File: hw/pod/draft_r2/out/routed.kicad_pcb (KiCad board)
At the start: 4 copper layers, 30 x 12 mm, 74 parts, among them J1 TestPoint_Pad_D1.0mm, J10 TestPoint_Pad_D1.0mm, J11 TestPoint_Pad_D1.0mm, J12 TestPoint_Pad_D1.0mm, J2 TestPoint_Pad_D1.0mm, J3 TestPoint_Pad_D1.0mm, J4 WirePad_1.0x2.0mm, J5 TestPoint_Pad_D1.0mm, J7 TestPoint_Pad_D1.0mm, J8 TestPoint_Pad_D1.0mm, J9 TestPoint_Pad_D1.0mm, Q1 Nexperia_SOT1216_DFN1010B-6, Q2 Nexperia_SOT1216_DFN1010B-6, SW1 SW-SMD_4P-L3.0-W2.6-P1.85-LS3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, U1 QFN-48-1EP_7x7mm_P0.5mm_EP5.6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, U2 Knowles_LGA-5_3.5x2.65mm, U3 DSBGA-8_L1.6-W0.9-R2-C4-P0.40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, U4 X2SON-4_L1.0-W1.0-P0.65-TL-EP, U6 SOT-553-5_L1.6-W1.2-P0.50-LS1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, Y1 Crystal_SMD_2012-2Pin_2.0x1.2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

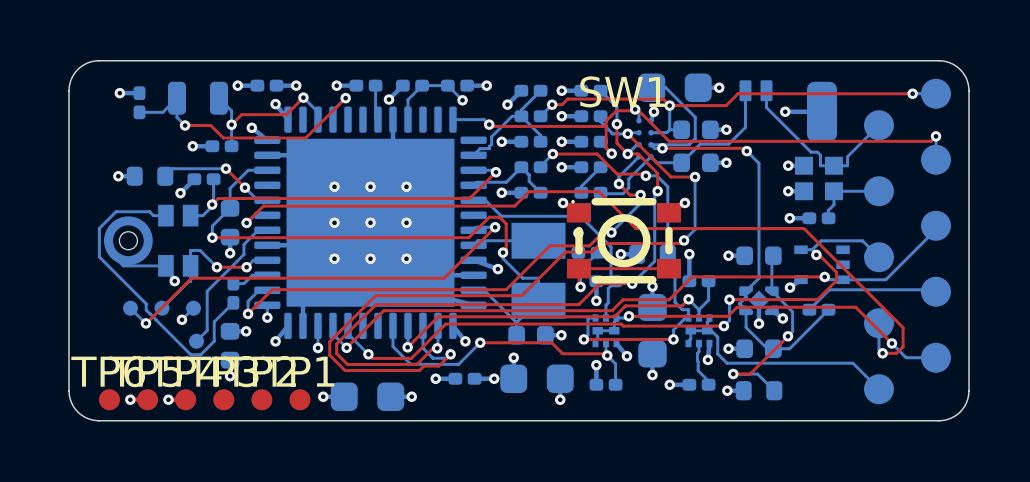
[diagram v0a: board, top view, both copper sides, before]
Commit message: Phase 2 route: 0.11 mm routing clearance for both FreeRouting passes (0.10 produced 0.192 mm hole clearance); routed board DRC 0 errors, 7 unconnected (U1 top-row escapes NRST/BTN/VBUS_SENSE + LSE_OUT, MDF_CCK, TP1/TP6): needs U1's top strip (C1/C10/C2/C3) loosened or hand routing
Co-Authored-By: Claude Opus 5.5 <noreply@anthropic.com>
Claude-Session: https://claude.ai/code/session_01Wg997D6KFs8bxoAH56jZZJ
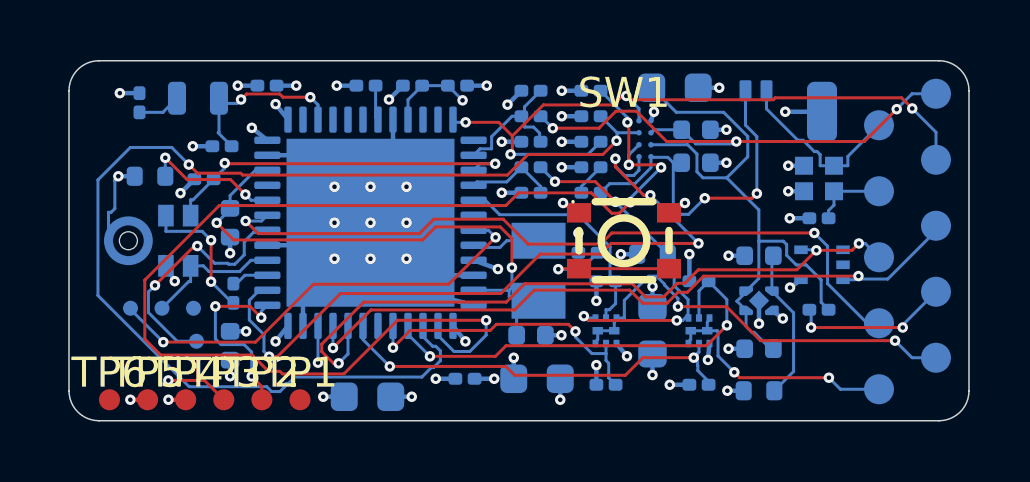
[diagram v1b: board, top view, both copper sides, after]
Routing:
- net I2C_SCL: track 23.8 -> 41.6 mm
- net GB_P: track 1.55 -> 13.9 mm, vias 0 -> 2
- net I2C_SDA: track 26.7 -> 38.9 mm, vias 4 -> 2
- net LSE_OUT: track 9.43 -> 1.44 mm, vias 2 -> 0
- net CHG_INT: track 18.2 -> 24.6 mm
- net SWCLK: track 0.41 -> 6.39 mm, vias 1 -> 3
- net MIC_CLK: track 10.5 -> 4.57 mm, vias 0 -> 2
- net VBUS: track 7.32 -> 11.7 mm, vias 0 -> 2
- net DBG_TX: track 4.86 -> 8.26 mm, vias 0 -> 2
- net TS: track 19.8 -> 23.2 mm
- net BRIDGE_RTN: track 14.7 -> 11.9 mm
- net LED_K: track 27.5 -> 24.8 mm
- net VSYS: track 17.4 -> 19.8 mm, vias 2 -> 0
- net VBAT: track 15.5 -> 17.8 mm
- net GB_N: track 12.6 -> 14.7 mm
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
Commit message: Phase 2 board lettering: silk.py reads the port/button/outline from the board (one-face board: name block between the mic-port motif and SW1, 'PHASE 2'); pin-1 dot list in a sidecar; place_r2 --route letters the fresh board. Known issue: manual re-runs on an already-lettered board can segfault in pcbnew's SWIG bindings (build scripts only letter fresh boards)
Co-Authored-By: Claude Opus 5.5 <noreply@anthropic.com>
Claude-Session: https://claude.ai/code/session_01Wg997D6KFs8bxoAH56jZZJ
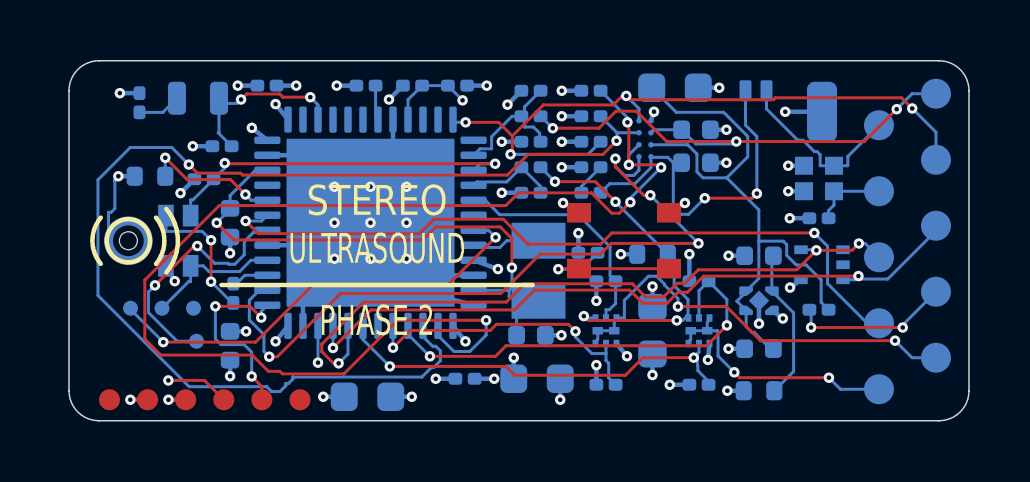
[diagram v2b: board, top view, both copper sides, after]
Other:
- board text added: "PHASE 2"
- board text added: "STEREO"
- board text added: "ULTRASOUND"

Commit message: Phase 2 route closure (agent v6): 1 unconnected (I2C_SCL at U1.26), DRC 0 errors, placement check pass: U1 top strip loosened (C2/C3/C10), C9 pocket fixed, Y1 vertical, TP3/TP6 moved on F; mic port now x 1.88 (shell_r2 re-check)
Co-Authored-By: Claude Opus 5.5 <noreply@anthropic.com>
Claude-Session: https://claude.ai/code/session_01Wg997D6KFs8bxoAH56jZZJ
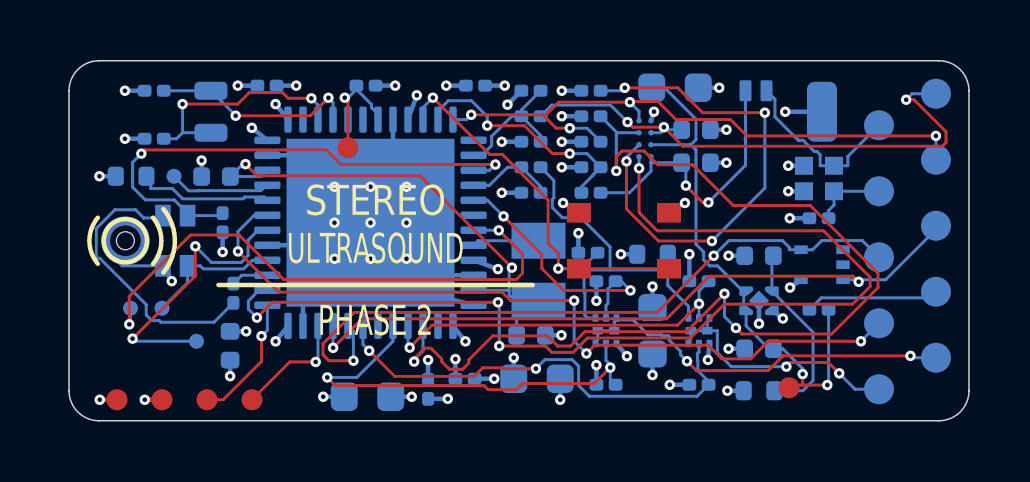
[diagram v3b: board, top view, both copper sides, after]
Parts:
- moved TP6 22.7 mm to (24.0, 10.9)
- moved C2 10.1 mm to (12.0, 10.9), turned to -90 degrees
- moved TP3 9.36 mm to (9.30, 2.90)
- moved TP8 4.45 mm to (3.50, 3.85)
- moved C11 2.27 mm to (2.84, 2.60)
- moved TP2 1.83 mm to (4.60, 11.3)
- moved C9 1.61 mm to (4.90, 3.86), turned to 180 degrees
- moved TP1 1.60 mm to (6.10, 11.3)
- moved C13 1.58 mm to (5.12, 5.40), turned to -90 degrees
- moved TP5 1.02 mm to (1.60, 11.3)
- moved TP4 0.79 mm to (3.10, 11.3)
- moved C12 0.63 mm to (2.84, 1.00), turned to 180 degrees
- moved R1 0.63 mm to (2.07, 3.85)
- moved Y1 0.62 mm to (4.73, 1.70), turned to 90 degrees
- moved C3 0.60 mm to (13.6, 0.83)
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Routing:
- net I2C_SCL: track 41.6 -> 16.5 mm, vias 5 -> 4
- net CHG_INT: track 24.6 -> 35.3 mm
- net BTN: track 5.24 -> 13.8 mm, vias 1 -> 2
- net VBUS_SENSE: track 1.12 -> 8.06 mm, vias 0 -> 2
- net MIC_VDD: track 12.1 -> 17.6 mm
- net LSE_OUT: track 1.44 -> 6.87 mm, vias 0 -> 2
- net MIC_CLK: track 4.57 -> 9.54 mm, vias 2 -> 0
- net GA_P: track 10.2 -> 14.6 mm
- net I2C_SDA: track 38.9 -> 34.6 mm, vias 2 -> 4
- net MDF_SDI: track 14.9 -> 18.7 mm
- net MDF_CCK: track 0.00 -> 3.39 mm
- net SWDIO: track 1.23 -> 3.88 mm
- net TS: track 23.2 -> 20.6 mm
- net GB_N: track 14.7 -> 12.4 mm
- net VBUS: track 11.7 -> 9.52 mm
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
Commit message: Phase 2 board fully routed: 0 unconnected, DRC 0. I2C_SCL at U1.26 (boxed in on both outer faces) bridged 8.97 mm on the In2 +3V0 plane by new hw/pod/inner_bridge.py (maze route, plane stays one island, -4 mm2). Pin swap ruled out from the DS AF table; ECR-0018 log + reg-board updated
Co-Authored-By: Claude Opus 5.5 <noreply@anthropic.com>
Claude-Session: https://claude.ai/code/session_01Wg997D6KFs8bxoAH56jZZJ
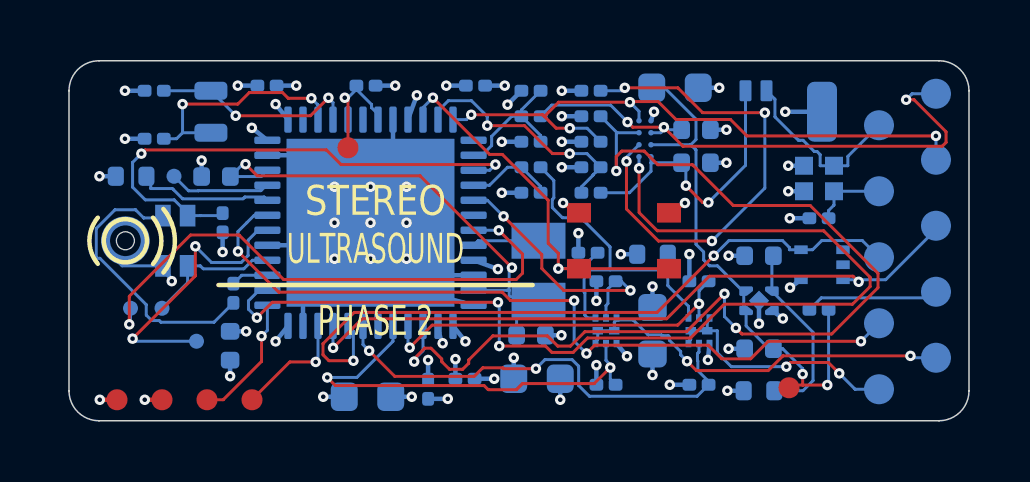
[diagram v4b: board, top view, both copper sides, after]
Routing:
- net I2C_SCL: track 16.5 -> 26.1 mm, vias 4 -> 5
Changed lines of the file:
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@@
+	)
+	(via
+		(at 12.455291 9.417055)
+		(size 0.35)
+		(drill 0.15)
+		(layers "F.Cu" "B.Cu")
+		(net "I2C_SCL")
 	)
 	(via
@@
 		(drill 0.15)
 		(layers "F.Cu" "B.Cu")
+		(net "I2C_SCL")
+	)
+	(segment
+		(start 12.3 8.8375)
+		(end 12.455291 9.417055)
+		(width 0.1)
+		(layer "B.Cu")
 		(net "I2C_SCL")
 	)
@@
 		(net "I2C_SCL")
 	)
+	(segment
+		(start 18.575 3.775)
+		(end 18.625 3.725)
+		(width 0.1)
+		(layer "In2.Cu")
+		(net "I2C_SCL")
+	)
+	(segment
+		(start 14.175 7.725)
+		(end 14.225 7.675)
+		(width 0.1)
+		(layer "In2.Cu")
+		(net "I2C_SCL")
+	)
+	(segment
+		(start 18.575 3.875)
+		(end 18.575 3.775)
+		(width 0.1)
+		(layer "In2.Cu")
+		(net "I2C_SCL")
+	)
+	(segment
+		(start 12.455291 9.417055)
+		(end 12.475 9.375)
+		(width 0.1)
+		(layer "In2.Cu")
+		(net "I2C_SCL")
+	)
+	(segment
+		(start 12.475 9.375)
+		(end 14.125 7.725)
+		(width 0.1)
+		(layer "In2.Cu")
+		(net "I2C_SCL")
+	)
+	(segment
+		(start 16.775 5.425)
+		(end 16.825 5.425)
+		(width 0.1)
+		(layer "In2.Cu")
+		(net "I2C_SCL")
+	)
+	(segment
+		(start 18.625 3.425)
+		(end 18.5827 3.353)
+		(width 0.1)
+		(layer "In2.Cu")
+		(net "I2C_SCL")
+	)
+	(segment
+		(start 14.125 7.725)
+		(end 14.175 7.725)
+		(width 0.1)
+		(layer "In2.Cu")
+		(net "I2C_SCL")
+	)
+	(segment
+		(start 14.225 7.675)
+		(end 14.525 7.675)
+		(width 0.1)
+		(layer "In2.Cu")
+		(net "I2C_SCL")
+	)
+	(segment
+		(start 17.075 5.375)
+		(end 18.575 3.875)
+		(width 0.1)
+		(layer "In2.Cu")
+		(net "I2C_SCL")
+	)
+	(segment
+		(start 14.525 7.675)
+		(end 16.775 5.425)
+		(width 0.1)
+		(layer "In2.Cu")
+		(net "I2C_SCL")
+	)
+	(segment
+		(start 16.875 5.375)
+		(end 17.075 5.375)
+		(width 0.1)
+		(layer "In2.Cu")
+		(net "I2C_SCL")
+	)
+	(segment
+		(start 16.825 5.425)
+		(end 16.875 5.375)
+		(width 0.1)
+		(layer "In2.Cu")
+		(net "I2C_SCL")
+	)
+	(segment
+		(start 18.625 3.725)
+		(end 18.625 3.425)
+		(width 0.1)
+		(layer "In2.Cu")
+		(net "I2C_SCL")
+	)

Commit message: LN-M03 Kelvin fix on the Phase-2 board: hw/pod/kelvin_r21.py (two pad-hugging GND vias at R21, 4 options scored). All layout-noise metrics now pass (M03 3.31 -> 1.29 %); DRC 0, 0 unconnected
Co-Authored-By: Claude Opus 5.5 <noreply@anthropic.com>
Claude-Session: https://claude.ai/code/session_01Wg997D6KFs8bxoAH56jZZJ
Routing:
- net GND: track 38.7 -> 38.9 mm, vias 48 -> 49
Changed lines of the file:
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@@
+	)
+	(via
+		(at 18.94 6.01)
+		(size 0.35)
+		(drill 0.15)
+		(layers "F.Cu" "B.Cu")
+		(net "GND")
+	)
+	(via
+		(at 18.55 6.45)
+		(size 0.35)
+		(drill 0.15)
+		(layers "F.Cu" "B.Cu")
+		(net "GND")
 	)
 	(via
@@
 	(via
 		(at 10.875 0.83)
-		(size 0.35)
-		(drill 0.15)
-		(layers "F.Cu" "B.Cu")
-		(net "GND")
-	)
-	(via
-		(at 18.395 6.45)
 		(size 0.35)
 		(drill 0.15)
@@
 	)
 	(segment
-		(start 18.94 6.45)
-		(end 18.395 6.45)
-		(width 0.15)
-		(layer "B.Cu")
-		(net "GND")
-	)
-	(segment
 		(start 10.22 0.83)
 		(end 10.875 0.83)
@@
 	)
 	(segment
+		(start 18.94 6.45)
+		(end 18.94 6.01)
+		(width 0.25)
+		(layer "B.Cu")
+		(net "GND")
+	)
+	(segment
 		(start 24.5 3.5)
 		(end 23.975 3.5)
@@
 		(layer "B.Cu")
 		(net "GND")
+	)
+	(segment
+		(start 18.94 6.45)
+		(end 18.55 6.45)
+		(width 0.25)
+		(layer "B.Cu")
+		(net "GND")

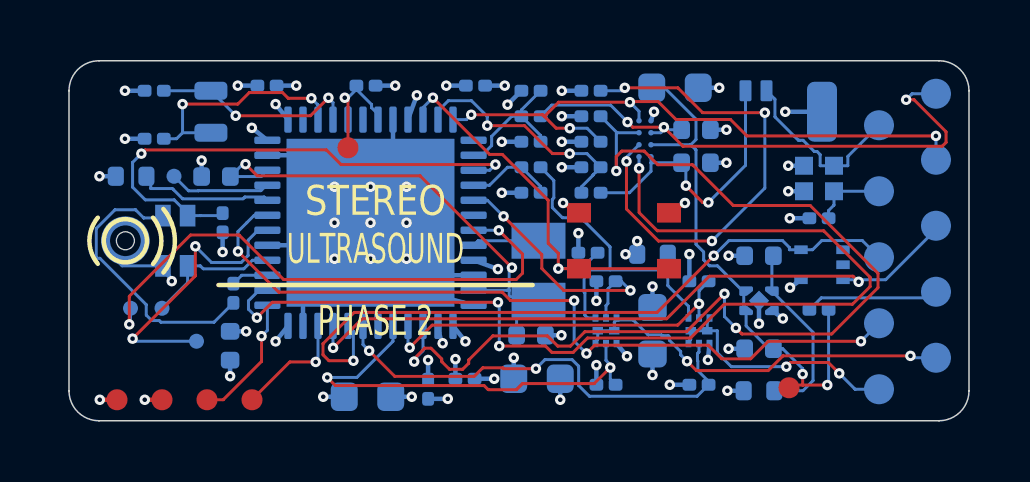
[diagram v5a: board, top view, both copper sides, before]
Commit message: Phase-2 board: B-DOC-AUDIT-0007 layout fixes 1-3 (local re-route of the committed board)
- J3 DOCK_VBUS / J4 GND swapped: J4 now sits between J3 and J5 VBAT (ASM-09); J3-J5 gap 1.17 -> 2.80 mm, all wire-pad gaps >= 0.90
- mic-port keep-out (R-ACO-P6): F.Cu rule area r 1.6 in place_r2 (FreeRouting + DRC enforce it), fan-out avoids it, check 'port';
  MDF_SDI re-routed: nearest F copper / via 1.35 -> 1.87 mm from the port
- LSE: Y1/C11/C12 moved, C1 to the QFN corner; LSE_IN/LSE_OUT pre-routed on B (locked), 0 vias, 7.72 / 7.43 mm (was 2 vias each, F+B)
- VDDA pin 9: C6 100 nF at the pin (1.13 mm, was 8.8), C5 1 uF 2.32 mm (was 9.2); C3 to VDD pin 36; C10 / R9 nudged; NEAR rules per pin
- R21 stays mid-board (MZD-4 not done): edge position scored LN-M03 2.48 % (limit 2) or an unroutable BRIDGE_RTN when flipped
- tools: place_r2 pre-routes / keep-out / --probe / --fr-args; local_reroute.py (move + rip + locked FreeRouting pass);
  fb_bridge.py (F+B maze, rip-and-repair); inner_bridge F/B layers + pads/rule areas as obstacles; kelvin_r21 reads the R21 pad
- DRC 0 / 0 unconnected; place_r2 check pass; LN M01..M05 26.5 / 20.1 / 1.29 % / 0.127 / 8.72 (unchanged); smoke exit 0

Co-Authored-By: Claude Opus 5.5 <noreply@anthropic.com>
Claude-Session: https://claude.ai/code/session_01Wg997D6KFs8bxoAH56jZZJ
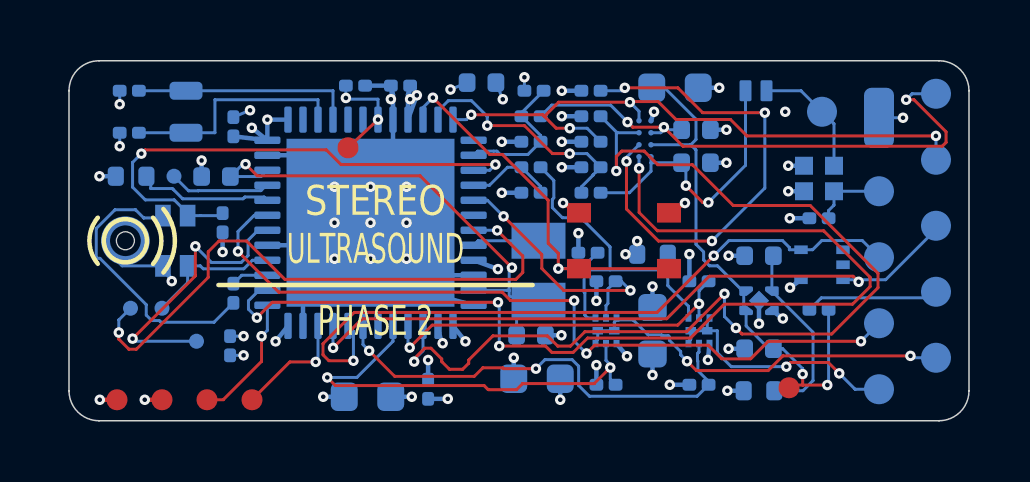
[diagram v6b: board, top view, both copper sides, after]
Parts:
- moved C5 12.1 mm to (13.8, 0.73), turned to 0 degrees
- moved C3 11.9 mm to (5.37, 9.50), turned to 90 degrees
- moved C6 10.0 mm to (11.1, 0.83)
- moved J3 1.95 mm to (25.1, 1.70)
- moved J4 1.91 mm to (27.0, 1.90)
- moved C1 1.77 mm to (5.48, 2.20), turned to 90 degrees
- moved C11 0.85 mm to (2.01, 2.40)
- moved Y1 0.83 mm to (3.90, 1.70)
- moved C12 0.83 mm to (2.01, 1.00)
- moved C10 0.35 mm to (9.55, 0.83)
- moved R9 0.10 mm to (15.5, 1.00)
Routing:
- net +3V0: track 15.7 -> 17.7 mm, vias 24 -> 23
- net DOCK_VBUS: track 6.09 -> 4.11 mm
- net MDF_SDI: track 18.7 -> 20.0 mm
- net LSE_OUT: track 6.87 -> 7.43 mm, vias 2 -> 0
- net LSE_IN: track 7.94 -> 7.73 mm, vias 2 -> 0
- net NRST: track 3.65 -> 3.57 mm, vias 1 -> 2

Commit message: RB-19: routed board Value fields now hold the schematic values (74/74 from pod_mz2.net via pcbnew); geometry untouched
git diff: only the 74 (property "Value" ...) lines. bom_check values WARN -> PASS.
DRC before/after identical: 0 errors, 3 pre-existing warnings (1 hole_to_hole, 2
via_dangling) -> new backlog item CHK-DRCWARN (router). plm 0/0/0/0.

Co-Authored-By: Claude Opus 5.5 <noreply@anthropic.com>
Claude-Session: https://claude.ai/code/session_01Wg997D6KFs8bxoAH56jZZJ
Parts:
- C1, C10, C13, C19, C2, C3, C6: value C_0201_0603Metric -> 100n
- C11, C12: value C_0201_0603Metric -> 8p2
- C14: value C_0603_1608Metric -> 22u
- C15: value C_0402_1005Metric -> 4u7 25V
- C16: value C_0402_1005Metric -> 4u7
- C17, C18, C5: value C_0402_1005Metric -> 1u
- C21, C4, C7: value C_0603_1608Metric -> 10u
- C22: value C_0201_0603Metric -> 10n
- C8, C9: value C_0402_1005Metric -> 2u2 10V
- D4: value D_SOD-882 -> PMEG3005EL
- D5, D6: value X1SON-2_L1.0-W0.6-P0.65-BI-1 -> TPD1E10B06DPYR
- J1: value TestPoint_Pad_D1.0mm -> XDCR_A
- J10: value TestPoint_Pad_D1.0mm -> D+
- J11: value TestPoint_Pad_D1.0mm -> D-
- J12: value TestPoint_Pad_D1.0mm -> CC
- J2: value TestPoint_Pad_D1.0mm -> XDCR_B
- J3: value TestPoint_Pad_D1.0mm -> VBUS
- J4: value WirePad_1.0x2.0mm -> GND
- J5: value TestPoint_Pad_D1.0mm -> BAT+
- J7: value TestPoint_Pad_D1.0mm -> LED+
- J8: value TestPoint_Pad_D1.0mm -> LED-
- J9: value TestPoint_Pad_D1.0mm -> NTC
- L1: value L0806 -> 2u2
- Q1, Q2: value Nexperia_SOT1216_DFN1010B-6 -> PMCXB290UE
- R1: value R_0402_1005Metric -> 10k
- R10, R14: value R_0201_0603Metric -> 2k2
- R12, R13, R3, R4, R5, R6: value R_0201_0603Metric -> 100k
- R15, R16: value R_0201_0603Metric -> 10k
- R18: value R_0201_0603Metric -> 5k1
- R2: value R_0201_0603Metric -> 33
- R20: value R_0402_1005Metric -> 0
- R21: value R_0402_1005Metric -> 0.1
- R22: value R_0201_0603Metric -> 1k
- R8, R9: value R_0201_0603Metric -> 1M
- RT1: value R_0201_0603Metric -> 10k B3435
- SW1: value SW-SMD_4P-L3.0-W2.6-P1.85-LS3.4 -> KMT022NGJLHS
- TP1: value TestPoint_Pad_D0.7mm -> SWDIO
- TP10: value TestDot_D0.5mm -> MIC_DATA
- TP2: value TestPoint_Pad_D0.7mm -> SWCLK
- TP3: value TestPoint_Pad_D0.7mm -> NRST
- TP4: value TestPoint_Pad_D0.7mm -> 3V0
- TP5: value TestPoint_Pad_D0.7mm -> GND
- TP6: value TestPoint_Pad_D0.7mm -> VSYS
- TP7: value TestDot_D0.5mm -> DBG_TX
- TP8: value TestDot_D0.5mm -> MDF_CCK
- TP9: value TestDot_D0.5mm -> MDF_SDI
- U1: value QFN-48-1EP_7x7mm_P0.5mm_EP5.6x5.6mm -> STM32U575CIUxQ
- U2: value Knowles_LGA-5_3.5x2.65mm -> SPH0641LU4H-1
- U3: value DSBGA-8_L1.6-W0.9-R2-C4-P0.40-BL -> BQ25180YBGR
- U4: value X2SON-4_L1.0-W1.0-P0.65-TL-EP -> TPS7A2030PDQNR
- U6: value SOT-553-5_L1.6-W1.2-P0.50-LS1.6-TL-1 -> TPD2E2U06DRLR
- Y1: value Crystal_SMD_2012-2Pin_2.0x1.2mm -> 32.768k 7pF

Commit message: CHK-DRCWARN: 2 dangling vias deleted from the routed board (pcbnew, authorised); DRC 0 errors / 0 unconnected / 1 warning; noise metrics identical
Deleted (only change to routed.kicad_pcb): GND via (23.875, 1.7), on the In1 plane with
no F/B copper; NRST via (9.23, 1.24), the locked pre-via place_r2.py adds for pin 7 ->
TP3, unused by the router (TP3 reached another way; next place_r2 run recreates it).
kicad-cli DRC with schematic parity: 0 errors, 0 unconnected, parity 0, 1 warning.
Remaining warning is real: hole_to_hole 0.109 mm between two +3V0 vias (11.37, 1.28) /
(11.595, 1.152), 0.259 c-c, D0.15 drills, rule 0.25: same net (harmless electrically),
drilling-web risk; fix at the next route touch (router).
Noise smoke before/after: LN-M01 26.5 dB, M02 20.1, M03 1.29 %, M04 0.1267 mV,
M05 8.718 uV, M06 0.1074 mV, identical; layout-noise.yaml board sha 9e762786 ->
36d088d4 (RB-19 values + these vias), vias 132 -> 130; smoke exit 0. plm 0/0/0/0.

Co-Authored-By: Claude Opus 5.5 <noreply@anthropic.com>
Claude-Session: https://claude.ai/code/session_01Wg997D6KFs8bxoAH56jZZJ
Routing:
- net NRST: vias 2 -> 1
- net GND: vias 49 -> 48
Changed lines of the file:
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@@
-	)
-	(via
-		(at 23.875 1.7)
-		(size 0.35)
-		(drill 0.15)
-		(layers "F.Cu" "B.Cu")
-		(net "GND")
 	)
 	(via
@@
 		(net "NRST")
 	)
-	(via
-		(at 9.23 1.24)
-		(size 0.35)
-		(drill 0.15)
-		(layers "F.Cu" "B.Cu")
-		(locked yes)
-		(net "NRST")
-	)
